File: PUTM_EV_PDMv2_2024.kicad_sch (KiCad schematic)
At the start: 11 parts, among them J5 FTSH-107-01-L-DV-K-A, J6 USB_B_Micro, J7 USB_C_Receptacle_USB2.0_14P, U1 STM32G0C1KCTxN

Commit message: Minor fixes
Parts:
- removed J5: FTSH-107-01-L-DV-K-A, FTSH-107-01-L-DV-K-A:FTSH-107-XX-YYY-DV-K-A, symbol ftsh-107-01-l-dv-k-a:FTSH-107-01-L-DV-K-A
- removed J6: USB_B_Micro, symbol Connector:USB_B_Micro
- removed R20: 100k, Resistor_SMD:R_0603_1608Metric, symbol Device:R_Small
- added C53: 10n, symbol Device:C_Small
- added J6: FTSH-107-01-L-DV-K-A, FTSH-107-XX-YYY-DV-K-A, symbol FTSH-107-01-L-DV-K-A:FTSH-107-01-L-DV-K-A
- added R22, R23: 5.1k, symbol Device:R_Small
- added R66: 100k, Resistor_SMD:R_0603_1608Metric, symbol Device:R_Small
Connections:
- net +3.3V: now also J6.3, R66.2
- net GND: now also C53.1, C53.2, J6.11, J6.5, J6.7, R22.1, R23.1
- net RST: now also J6.12, R66.1
- net SWCLK: now also J6.6
- net SWDIO: now also J6.4
- net USART1_RX: now also J6.13
- net USART1_TX: now also J6.14
- net at J7.A5 (CC1): now also R22.2
- net D+: now reaches J7.A6 (D+)
- net D+: now also J7.B6 (D+), U1.23 (PA12/PA10)
- net D-: now reaches J7.A7 (D-)
- net D-: now also J7.B7 (D-), U1.22 (PA11/PA9)
- net at J7.B5 (CC2): now also R23.2
- net CSN renamed SPI1_NSS
- net IS_1 renamed FUSE1_IS
- net IS_2 renamed FUSE2_IS
- net IS_3 renamed FUSE3_IS
- net IS_4 renamed FUSE4_IS
- net LED_1 renamed LED1
- net LED_2 renamed LED2
- net LED_3 renamed LED3
- net LED_4 renamed LED4
- net MISO renamed SPI1_MISO
- net MOSI renamed SPI1_MOSI
- net SCLK renamed SPI1_SCK
- no-connect marks 10 -> 9
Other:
- sheet CAN ports: added CAN_H, CAN_L, CAN_RX, CAN_TX; removed none
- sheet Controllers ports: added CSN, IS_1, IS_2, IS_3, IS_4, LHI_1, LHI_2, LHI_3, LHI_4, MISO, MOSI, SCLK; removed none
- sheet LEDs ports: added LED_1, LED_2, LED_3, LED_4; removed none
- note added: "USB C connector"
- note added: "csc"
- note added: "sclk"
- note removed: "?"
- note removed: "PA11/12"
- note removed: "check resistor"
- note removed: "usb connections"
- note removed: "usb dm"
- note removed: "usb dp"

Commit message: Footprint changes + started PCB
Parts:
- C53: footprint (none) -> Capacitor_SMD:C_0603_1608Metric_Pad1.08x0.95mm_HandSolder
- R22, R23: footprint (none) -> Resistor_SMD:R_0603_1608Metric_Pad0.98x0.95mm_HandSolder
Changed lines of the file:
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@@
 			)
 		)
-		(property "Footprint" ""
+		(property "Footprint" "Resistor_SMD:R_0603_1608Metric_Pad0.98x0.95mm_HandSolder"
 			(at 233.68 59.69 0)
 			(effects
@@
 			)
 		)
-		(property "Footprint" ""
+		(property "Footprint" "Resistor_SMD:R_0603_1608Metric_Pad0.98x0.95mm_HandSolder"
 			(at 233.68 57.15 0)
 			(effects
@@
 			)
 		)
-		(property "Footprint" ""
+		(property "Footprint" "Capacitor_SMD:C_0603_1608Metric_Pad1.08x0.95mm_HandSolder"
 			(at 262.89 93.98 0)
 			(effects

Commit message: Minor changes
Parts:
- removed FB1: BLM18SP102SZ1D, Inductor_SMD:L_0603_1608Metric, symbol Device:FerriteBead_Small
- added R20: 0, Resistor_SMD:R_0603_1608Metric_Pad0.98x0.95mm_HandSolder, symbol Device:R_Small
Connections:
- net +3.3V: now also R20.1
- net GND: no longer C53.1, J7.S1 (SHIELD)
- net STM_VCC: now also R20.2
- new net: C53.1, J7.S1 (SHIELD)
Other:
- note added: "CAN"
- note added: "Connectors"
- note added: "LEDs"
- note added: "Power"
- note added: "Power ICs"
- note added: "STM32"
- note removed: "csc"
- note removed: "sclk"

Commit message: Layout done
Added layout
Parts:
- removed R66: 100k, Resistor_SMD:R_0603_1608Metric, symbol Device:R_Small
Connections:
- net RST is gone; now on net NRST: J6.12
- net LED1: now also U1.21 (PA10/UCPD1_DBCC2); no longer U1.19 (PA9/UCPD1_DBCC1)
- net LED2: now also U1.19 (PA9/UCPD1_DBCC1); no longer U1.18 (PA8)
- net LED3: now also U1.18 (PA8); no longer U1.17 (PB15)
- net LED4: now also U1.17 (PB15); no longer U1.21 (PA10/UCPD1_DBCC2)
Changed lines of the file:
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@@
 	)
 	(junction
+		(at 144.78 78.74)
+		(diameter 0)
+		(color 0 0 0 0)
+	)
+	(junction
 		(at 149.86 67.31)
 		(diameter 0)
@@
 	(wire
 		(pts
-			(xy 143.51 78.74) (xy 156.21 78.74)
+			(xy 143.51 78.74) (xy 144.78 78.74)
 		)
 		(stroke
@@
 	(wire
 		(pts
+			(xy 259.08 132.08) (xy 260.35 132.08)
+		)
+		(stroke
+			(width 0)
+			(type default)
+		)
+	)
+	(wire
+		(pts
 			(xy 194.31 96.52) (xy 195.58 96.52)
 		)
@@
 	(wire
 		(pts
+			(xy 144.78 78.74) (xy 156.21 78.74)
+		)
+		(stroke
+			(width 0)
+			(type default)
+		)
+	)
+	(wire
+		(pts
 			(xy 255.27 96.52) (xy 259.08 96.52)
 		)
@@
 	(wire
 		(pts
+			(xy 144.78 74.93) (xy 144.78 78.74)
+		)
+		(stroke
+			(width 0)
+			(type default)
+		)
+	)
+	(wire
+		(pts
 			(xy 194.31 109.22) (xy 195.58 109.22)
 		)
@@
 	(wire
 		(pts
-			(xy 269.24 132.08) (xy 270.51 132.08)
-		)
-		(stroke
-			(width 0)
-			(type default)
-		)
-	)
-	(wire
-		(pts
-			(xy 259.08 132.08) (xy 264.16 132.08)
-		)
-		(stroke
-			(width 0)
-			(type default)
-		)
-	)
-	(wire
-		(pts
 			(xy 162.56 54.61) (xy 168.91 54.61)
 		)
@@
 	)
 	(label "LED1"
-		(at 195.58 101.6 0)
+		(at 195.58 104.14 0)
 		(fields_autoplaced yes)
 		(effects
@@
 	)
 	(label "LED2"
-		(at 195.58 99.06 0)
+		(at 195.58 101.6 0)
 		(fields_autoplaced yes)
 		(effects
@@
 	)
 	(label "LED4"
-		(at 195.58 104.14 0)
+		(at 154.94 119.38 180)
 		(fields_autoplaced yes)
 		(effects
@@
 				(size 1.27 1.27)
 			)
-			(justify left bottom)
+			(justify right bottom)
 		)
 	)
@@
 		)
 	)
+	(label "RST"
+		(at 144.78 74.93 0)
+		(fields_autoplaced yes)
+		(effects
+			(font
+				(size 1.27 1.27)
+			)
+			(justify left bottom)
+		)
+	)
 	(label "D-"
 		(at 233.68 67.31 0)
@@
 	)
 	(label "LED3"
-		(at 154.94 119.38 180)
+		(at 195.58 99.06 0)
 		(fields_autoplaced yes)
 		(effects
@@
 				(size 1.27 1.27)
 			)
-			(justify right bottom)
+			(justify left bottom)
 		)
 	)
@@
 	)
 	(symbol
-		(lib_id "Device:R_Small")
-		(at 266.7 132.08 90)
-		(unit 1)
-		(exclude_from_sim no)
-		(in_bom yes)
-		(on_board yes)
-		(dnp no)
-		(property "Reference" "R66"
-			(at 266.7 137.0584 90)
-			(effects
-				(font
-					(size 1.27 1.27)
-				)
-			)
-		)
-		(property "Value" "100k"
-			(at 266.7 134.747 90)
-			(effects
-				(font
-					(size 1.27 1.27)
-				)
-			)
-		)
-		(property "Footprint" "Resistor_SMD:R_0603_1608Metric"
-			(at 266.7 132.08 0)
-			(effects
-				(font
-					(size 1.27 1.27)
-				)
-				(hide yes)
-			)
-		)
-		(property "Datasheet" "~"
-			(at 266.7 132.08 0)
-			(effects
-				(font
-					(size 1.27 1.27)
-				)
-				(hide yes)
-			)
-		)
-		(property "Description" ""
-			(at 266.7 132.08 0)
-			(effects
-				(font
-					(size 1.27 1.27)
-				)
-				(hide yes)
-			)
-		)
-		(property "m" "667-ERJ-3EKF1003V"
-			(at 266.7 132.08 90)
-			(effects
-				(font
-					(size 1.27 1.27)
-				)
-				(hide yes)
-			)
-		)
-		(pin "1"
-		)
-		(pin "2"
-		)
-		(instances
-			(project "PUTM_EV_PDMv2_2024"
-				(path "/b652b05a-4e3d-4ad1-b032-18886abe7d45"
-					(reference "R66")
-					(unit 1)
-				)
-			)
-		)
-	)
-	(symbol
 		(lib_id "power:+3.3V")
 		(at 138.43 78.74 90)
@@
 					(unit 1)
 				)
-			)
-		)
-	)
-	(symbol
-		(lib_id "power:+3.3V")
-		(at 270.51 132.08 0)
-		(unit 1)
-		(exclude_from_sim no)
-		(in_bom yes)
-		(on_board yes)
-		(dnp no)
-		(property "Reference" "#PWR017"
-			(at 270.51 135.89 0)
-			(effects
-				(font
-					(size 1.27 1.27)
-				)
-				(hide yes)
-			)
-		)
-		(property "Value" "+3.3V"
-			(at 270.51 127.508 0)
-			(effects
-				(font
-					(size 1.27 1.27)
-				)
-			)
-		)
-		(property "Footprint" ""
-			(at 270.51 132.08 0)
-			(effects
-				(font
-					(size 1.27 1.27)
-				)
-				(hide yes)
-			)
-		)
-		(property "Datasheet" ""
-			(at 270.51 132.08 0)
-			(effects
-				(font
-					(size 1.27 1.27)
-				)
-				(hide yes)
-			)
-		)
-		(property "Description" ""
-			(at 270.51 132.08 0)
-			(effects
-				(font
-					(size 1.27 1.27)
-				)
-				(hide yes)
-			)
-		)
-		(pin "1"
-		)
-		(instances
-			(project "PUTM_EV_PDMv2_2024"
-				(path "/b652b05a-4e3d-4ad1-b032-18886abe7d45"
-					(reference "#PWR017")
-					(unit 1)
-				)

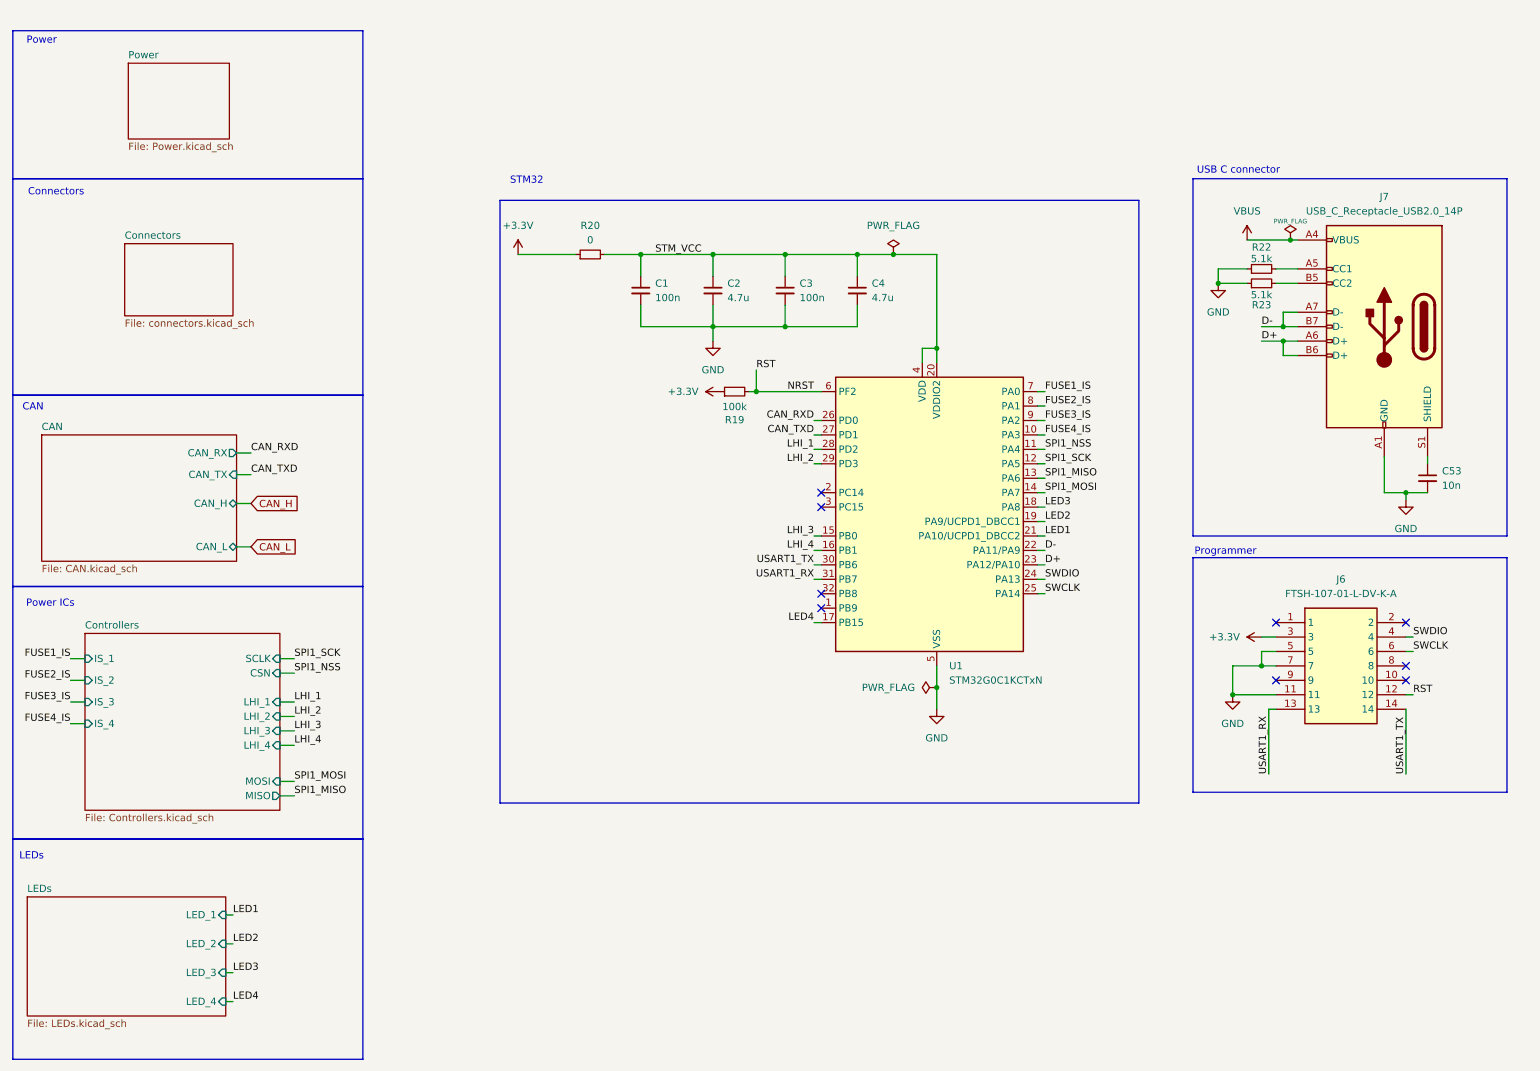
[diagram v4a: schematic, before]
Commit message: Minor fixes
added USBc tvs
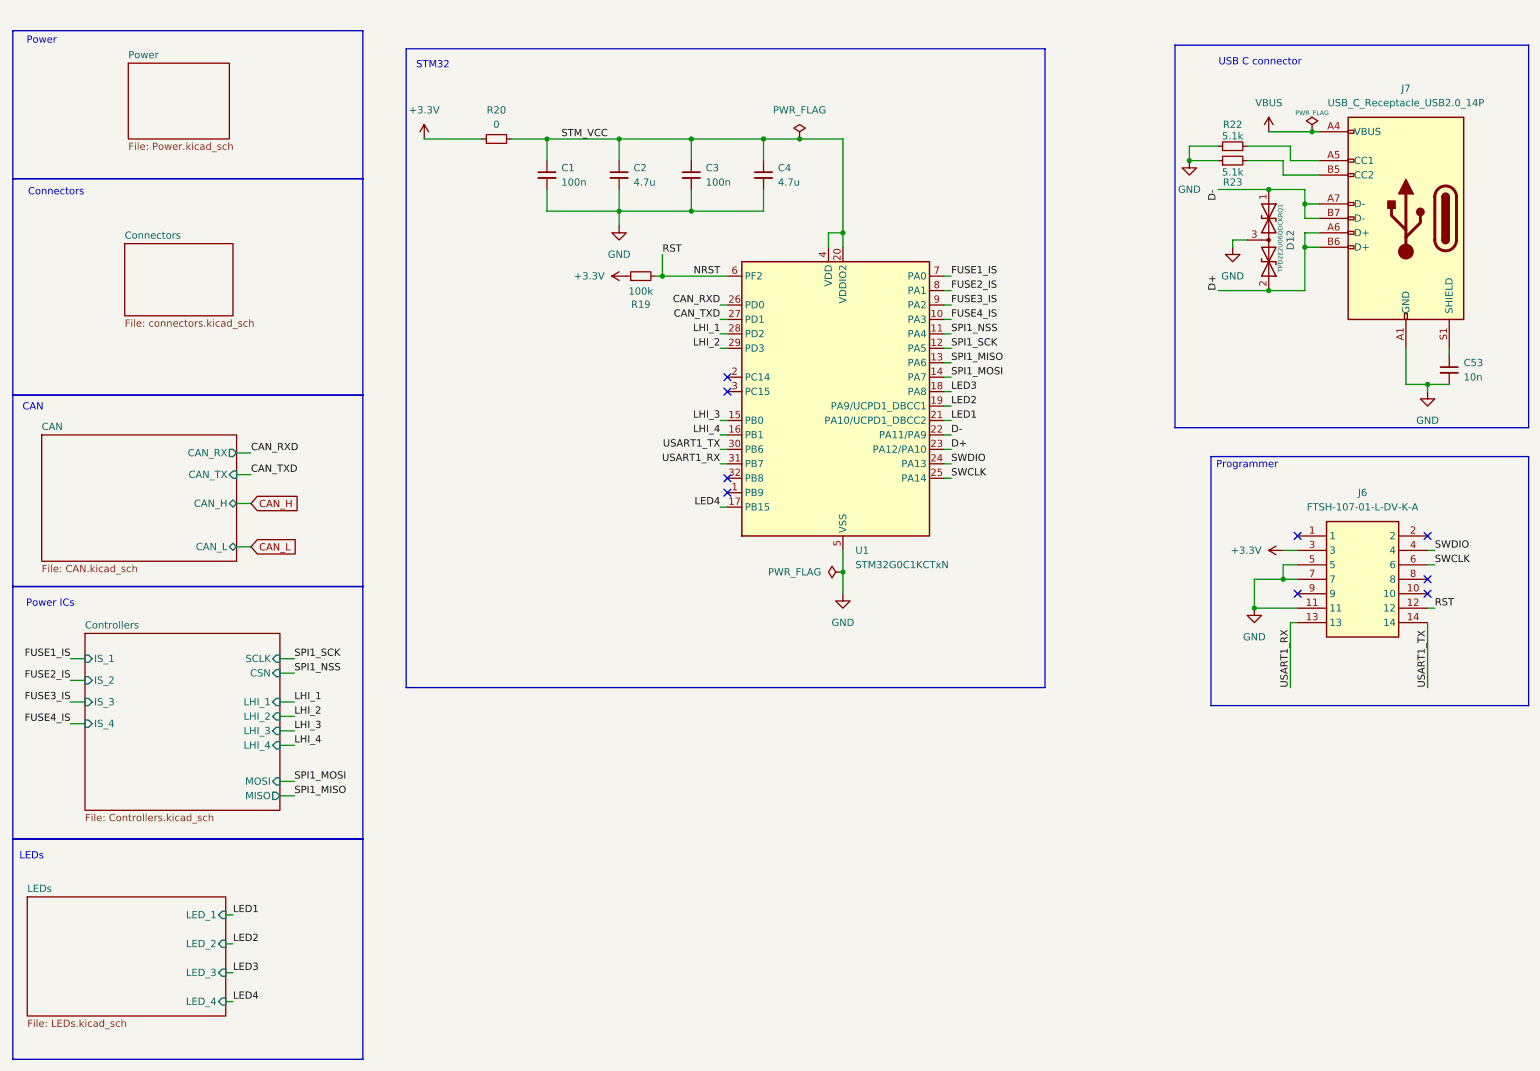
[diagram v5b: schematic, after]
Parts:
- added D12: TPD2E2U06QDCKRQ1, Package_TO_SOT_SMD:SOT-323_SC-70_Handsoldering, symbol Device:D_TVS_Dual_AAC
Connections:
- net D+: now also D12.2 (A2)
- net D-: now also D12.1 (A1)
- net GND: now also D12.3 (common)
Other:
- moved on the sheet: C1, C2, C3, C4, C53, J6, J7, R19, R20, R22, R23, U1
